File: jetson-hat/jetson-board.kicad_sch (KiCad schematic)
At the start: 2 parts, among them J1 GPIO, U1 SC16IS752IPW

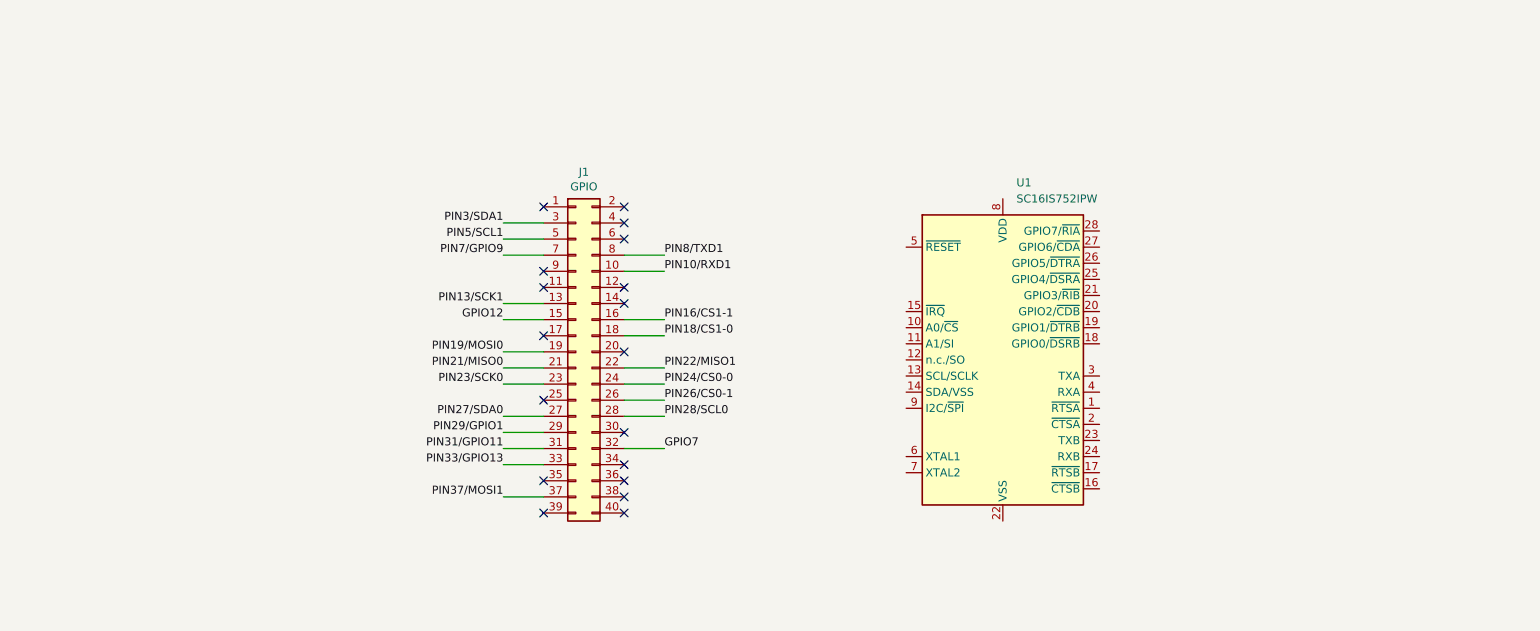
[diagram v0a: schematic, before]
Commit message: Connect JetHeader to Protocol Converter, LED, Button, Molex Headers
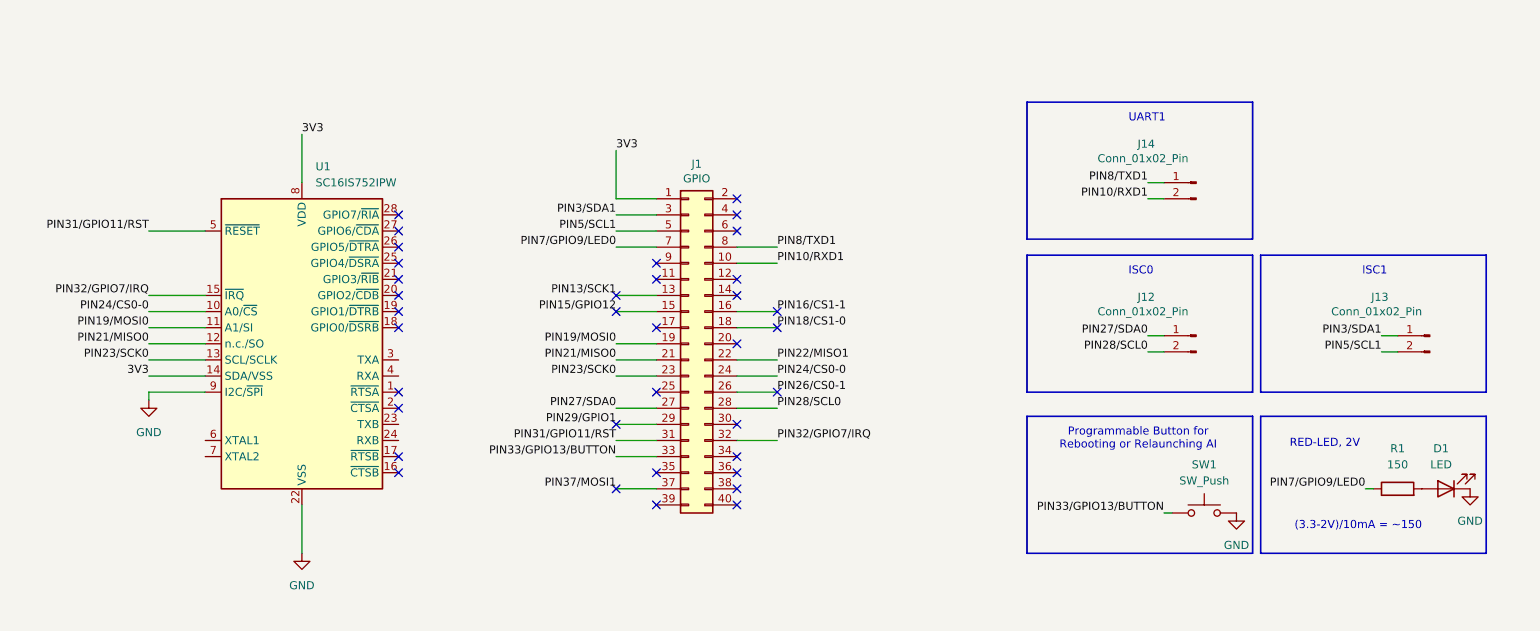
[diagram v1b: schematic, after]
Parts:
- added D1: LED, LED_SMD:LED_0805_2012Metric_Pad1.15x1.40mm_HandSolder, symbol Device:LED
- added J12, J13, J14: Conn_01x02_Pin, Connector_Molex:Molex_Mini-Fit_Jr_5566-02A_2x01_P4.20mm_Vertical, symbol Connector:Conn_01x02_Pin
- added R1: 150, Resistor_SMD:R_1206_3216Metric_Pad1.30x1.75mm_HandSolder, symbol Device:R
- added SW1: SW_Push, Button_Switch_THT:SW_NKK_GW12LJP, symbol Switch:SW_Push
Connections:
- net GPIO7 is gone; now on net PIN32/GPIO7/IRQ: J1.32 (Pin_32)
- net PIN31/GPIO11 is gone; now on net PIN31/GPIO11/RST: J1.31 (Pin_31)
- net PIN10/RXD1: now also J14.2 (Pin_2)
- net PIN19/MOSI0: now also U1.11 (A1/SI)
- net PIN21/MISO0: now also U1.12 (n.c./SO)
- net PIN23/SCK0: now also U1.13 (SCL/SCLK)
- net PIN24/CS0-0: now also U1.10 (A0/~{CS})
- net PIN27/SDA0: now also J12.1 (Pin_1)
- net PIN28/SCL0: now also J12.2 (Pin_2)
- net PIN3/SDA1: now also J13.1 (Pin_1)
- net PIN5/SCL1: now also J13.2 (Pin_2)
- net PIN8/TXD1: now also J14.1 (Pin_1)
- net 3V3: now reaches J1.1 (Pin_1)
- net 3V3: now also U1.14 (SDA/VSS), U1.8 (VDD)
- net PIN32/GPIO7/IRQ: now reaches U1.15 (~{IRQ})
- net GND: now reaches U1.22 (VSS)
- net GND: now also U1.9 (I2C/~{SPI}), D1.1 (K), SW1.2
- net PIN31/GPIO11/RST: now reaches U1.5 (~{RESET})
- net GPIO12 renamed PIN15/GPIO12
- net PIN33/GPIO13 renamed PIN33/GPIO13/BUTTON
- net PIN33/GPIO13/BUTTON: now also SW1.1
- net PIN7/GPIO9 renamed PIN7/GPIO9/LED0
- net PIN7/GPIO9/LED0: now also R1.1
- new net: D1.2 (A), R1.2
- no-connect marks 18 -> 36
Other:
- note added: "(3.3-2V)/10mA = ~150"
- note added: "ISC0"
- note added: "ISC1"
- note added: "Programmable Button for Rebooting or Relaunching AI"
- note added: "RED-LED, 2V"
- note added: "UART1"
- moved on the sheet: J1, U1

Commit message: Add crystal oscillator and UART connectors
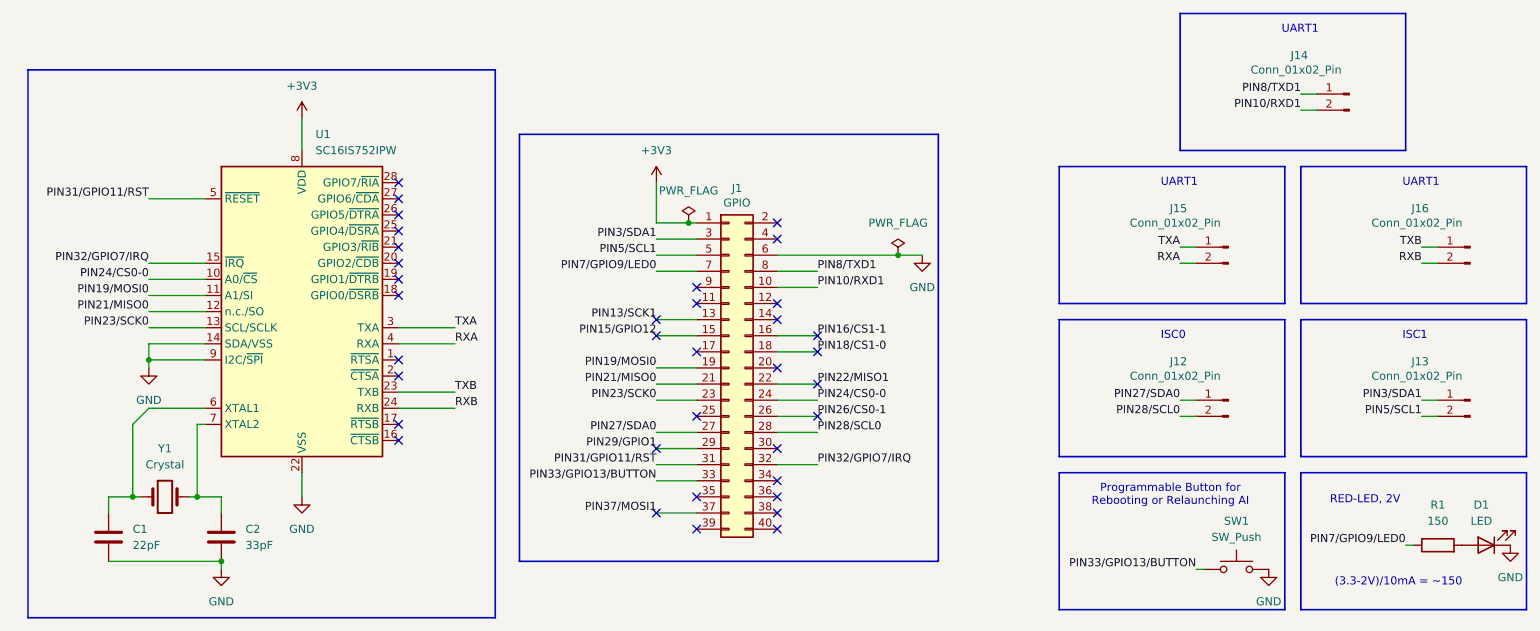
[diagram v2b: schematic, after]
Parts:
- added C1: 22pF, symbol Device:C
- added C2: 33pF, symbol Device:C
- added J15, J16: Conn_01x02_Pin, Connector_Molex:Molex_Mini-Fit_Jr_5566-02A_2x01_P4.20mm_Vertical, symbol Connector:Conn_01x02_Pin
- added Y1: Crystal, symbol Device:Crystal
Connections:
- net GND: now also J1.6 (Pin_6), U1.14 (SDA/VSS), C1.2, C2.2
- net TXB: now reaches U1.23 (TXB)
- net TXB: now also J16.1 (Pin_1)
- net RXB: now reaches U1.24 (RXB)
- net RXB: now also J16.2 (Pin_2)
- net TXA: now reaches U1.3 (TXA)
- net TXA: now also J15.1 (Pin_1)
- net RXA: now reaches U1.4 (RXA)
- net RXA: now also J15.2 (Pin_2)
- net at U1.6 (XTAL1): now also C1.1, Y1.1
- net at U1.7 (XTAL2): now also C2.1, Y1.2
- net 3V3 renamed +3V3
- net +3V3: no longer U1.14 (SDA/VSS)
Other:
- company: (none) -> Computer Science House
- title: (none) -> Bits N' Bytes Jetson
- moved on the sheet: D1, J1, J12, J13, J14, R1, SW1, U1

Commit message: Begin layout for Jetson
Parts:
- C1, C2: footprint (none) -> Capacitor_SMD:C_1206_3216Metric_Pad1.33x1.80mm_HandSolder
- Y1: footprint (none) -> Crystal:Crystal_SMD_5032-2Pin_5.0x3.2mm_HandSoldering
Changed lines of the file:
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@@
 			)
 		)
-		(property "Footprint" ""
+		(property "Footprint" "Capacitor_SMD:C_1206_3216Metric_Pad1.33x1.80mm_HandSolder"
 			(at 42.8752 133.35 0)
 			(hide yes)
@@
 			)
 		)
-		(property "Footprint" ""
+		(property "Footprint" "Crystal:Crystal_SMD_5032-2Pin_5.0x3.2mm_HandSoldering"
 			(at 50.8 123.19 0)
 			(hide yes)
@@
 			)
 		)
-		(property "Footprint" ""
+		(property "Footprint" "Capacitor_SMD:C_1206_3216Metric_Pad1.33x1.80mm_HandSolder"
 			(at 60.6552 133.35 0)
 			(hide yes)
